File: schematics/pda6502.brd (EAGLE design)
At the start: 100 x 80 mm, 34 parts, among them IC1 74HC00D, IC2 74HC138D, IC3 DS1813-SMD, J1 CON_HEADER_2X07-PTH, U1 W65C02S, U2 W65C22S, U3 28C256, U4 UM61256AK-12

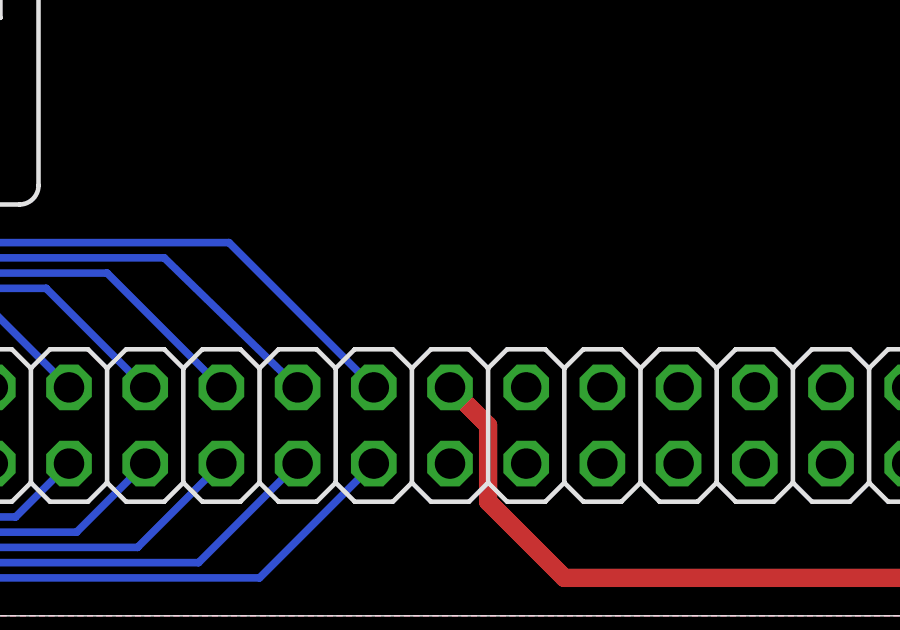
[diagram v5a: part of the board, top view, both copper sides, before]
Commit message: schematic, board: added 0.1 uF cap on 5V expansion pin 20.
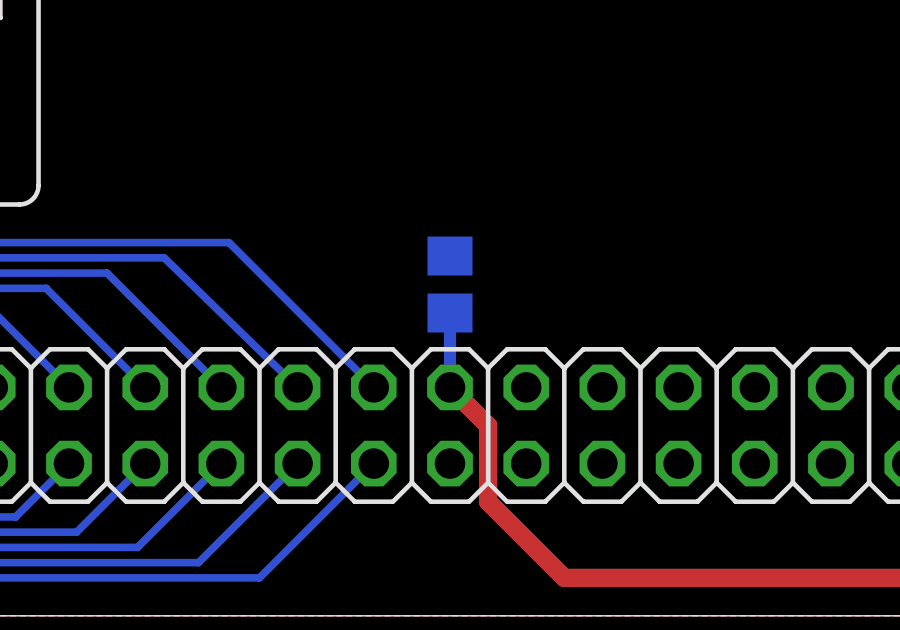
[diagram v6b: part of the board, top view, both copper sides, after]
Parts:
- added C14: 0.1μF, rcl:C0805
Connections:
- net 5V: now also C14.2
- net GND: now also C14.1
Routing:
- net 5V: track 398.3 -> 400.8 mm
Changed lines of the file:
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@@
 <element name="JP6" library="adafruit" package="2X20" value="EXPANSION" x="49.53" y="6.35"/>
 <element name="C13" library="rcl" package="C0805" value="0.1μF" x="76.962" y="5.08" rot="MR0"/>
+<element name="C14" library="rcl" package="C0805" value="0.1μF" x="48.26" y="11.049" rot="MR270"/>
 </elements>
 <signals>
@@
 <vertex x="100.33" y="80.01"/>
 </polygon>
-<wire x1="97.57" y1="69.85" x2="95.25" y2="60.96" width="0" layer="19" extent="1-1"/>
+<contactref element="C14" pad="1"/>
+<wire x1="95.25" y1="60.96" x2="97.57" y2="69.85" width="0" layer="19" extent="1-1"/>
+<wire x1="88.331" y1="60.96" x2="95.25" y2="60.96" width="0" layer="19" extent="16-16"/>
+<wire x1="81.28" y1="55.88" x2="88.331" y2="60.96" width="0" layer="19" extent="16-16"/>
+<wire x1="90.17" y1="77.8" x2="97.57" y2="69.85" width="0" layer="19" extent="1-1"/>
+<wire x1="85.09" y1="77.8" x2="90.17" y2="77.8" width="0" layer="19" extent="1-1"/>
+<wire x1="72.36" y1="76.065" x2="85.09" y2="77.8" width="0" layer="19" extent="1-1"/>
+<wire x1="66.675" y1="63.754" x2="72.39" y2="72.39" width="0" layer="19" extent="1-1"/>
+<wire x1="62.4" y1="67.31" x2="66.675" y2="63.754" width="0" layer="19" extent="1-1"/>
+<wire x1="48.26" y1="64.45" x2="62.4" y2="67.31" width="0" layer="19" extent="1-16"/>
+<wire x1="51.562" y1="51.877" x2="48.26" y2="64.45" width="0" layer="19" extent="16-16"/>
+<wire x1="47.051" y1="45.72" x2="51.562" y2="51.877" width="0" layer="19" extent="16-16"/>
+<wire x1="57.6834" y1="43.815" x2="51.562" y2="51.877" width="0" layer="19" extent="16-16"/>
+<wire x1="57.6834" y1="42.545" x2="57.6834" y2="43.815" width="0" layer="19" extent="16-16"/>
+<wire x1="57.6834" y1="38.735" x2="57.6834" y2="42.545" width="0" layer="19" extent="16-16"/>
+<wire x1="51.562" y1="35.748" x2="57.6834" y2="38.735" width="0" layer="19" extent="16-16"/>
+<wire x1="57.6834" y1="24.13" x2="51.562" y2="35.748" width="0" layer="19" extent="16-16"/>
+<wire x1="92.71" y1="45.72" x2="81.28" y2="55.88" width="0" layer="19" extent="1-1"/>
+<wire x1="95.25" y1="41.341" x2="92.71" y2="45.72" width="0" layer="19" extent="16-16"/>
+<wire x1="95.25" y1="38.1" x2="95.25" y2="41.341" width="0" layer="19" extent="16-16"/>
+<wire x1="90.744" y1="35.56" x2="95.25" y2="38.1" width="0" layer="19" extent="16-16"/>
+<wire x1="80.01" y1="31.75" x2="90.744" y2="35.56" width="0" layer="19" extent="16-16"/>
+<wire x1="75.057" y1="22.667" x2="80.01" y2="31.75" width="0" layer="19" extent="16-16"/>
+<wire x1="73.66" y1="7.62" x2="75.057" y2="22.667" width="0" layer="19" extent="16-16"/>
+<wire x1="77.912" y1="5.08" x2="73.66" y2="7.62" width="0" layer="19" extent="16-16"/>
+<wire x1="60.96" y1="7.62" x2="73.66" y2="7.62" width="0" layer="19" extent="1-1"/>
+<wire x1="55.88" y1="7.62" x2="60.96" y2="7.62" width="0" layer="19" extent="1-1"/>
+<wire x1="53.34" y1="7.62" x2="55.88" y2="7.62" width="0" layer="19" extent="1-1"/>
+<wire x1="50.8" y1="7.62" x2="53.34" y2="7.62" width="0" layer="19" extent="1-1"/>
+<wire x1="48.26" y1="5.08" x2="50.8" y2="7.62" width="0" layer="19" extent="1-1"/>
+<wire x1="35.494" y1="29.21" x2="51.562" y2="35.748" width="0" layer="19" extent="16-16"/>
+<wire x1="24.13" y1="31.75" x2="35.494" y2="29.21" width="0" layer="19" extent="16-16"/>
+<wire x1="21.59" y1="19.05" x2="24.13" y2="31.75" width="0" layer="19" extent="1-1"/>
+<wire x1="24.13" y1="16.51" x2="21.59" y2="19.05" width="0" layer="19" extent="1-1"/>
+<wire x1="25.4" y1="7.62" x2="24.13" y2="16.51" width="0" layer="19" extent="1-1"/>
+<wire x1="10.226" y1="29.21" x2="24.13" y2="31.75" width="0" layer="19" extent="16-16"/>
+<wire x1="10.16" y1="53.34" x2="10.226" y2="29.21" width="0" layer="19" extent="16-16"/>
+<wire x1="5.08" y1="62.23" x2="10.16" y2="53.34" width="0" layer="19" extent="1-1"/>
+<wire x1="5.08" y1="71.12" x2="5.08" y2="62.23" width="0" layer="19" extent="1-1"/>
+<wire x1="15.24" y1="74.93" x2="5.08" y2="71.12" width="0" layer="19" extent="1-1"/>
+<wire x1="48.26" y1="11.999" x2="25.4" y2="7.62" width="0" layer="19" extent="1-1"/>
 </signal>
 <signal name="5V">
@@
 <wire x1="76.2" y1="17.78" x2="76.2" y2="15.24" width="0.6096" layer="1"/>
 <wire x1="82.55" y1="16.51" x2="82.55" y2="8.89" width="0.3048" layer="1"/>
-<wire x1="96.52" y1="7.62" x2="93.98" y2="7.62" width="0" layer="19" extent="1-16"/>
 <wire x1="92.71" y1="3.81" x2="90.17" y2="1.27" width="0.6096" layer="1"/>
-<wire x1="93.98" y1="7.62" x2="92.71" y2="6.35" width="0" layer="19" extent="1-16"/>
 <wire x1="82.55" y1="8.89" x2="90.17" y2="1.27" width="0.6096" layer="1"/>
 <wire x1="76.012" y1="5.08" x2="73.66" y2="5.08" width="0.4064" layer="16"/>
@@
 <wire x1="95.25" y1="35.56" x2="96.52" y2="35.56" width="0.6096" layer="1"/>
 <wire x1="96.52" y1="35.56" x2="97.79" y2="36.83" width="0.6096" layer="1"/>
+<wire x1="92.71" y1="3.81" x2="92.71" y2="5.08" width="0.6096" layer="1"/>
+<wire x1="96.52" y1="7.62" x2="95.25" y2="7.62" width="0.6096" layer="1"/>
+<wire x1="92.71" y1="5.08" x2="95.25" y2="7.62" width="0.6096" layer="1" curve="-90"/>
+<contactref element="C14" pad="2"/>
+<wire x1="48.26" y1="10.099" x2="48.26" y2="7.62" width="0.4064" layer="16"/>
 <wire x1="29.21" y1="34.29" x2="31.75" y2="29.21" width="0" layer="19" extent="1-1"/>
 <wire x1="21.59" y1="28.106" x2="26.67" y2="34.29" width="0" layer="19" extent="16-16"/>
 <wire x1="13.97" y1="29.21" x2="21.59" y2="28.106" width="0" layer="19" extent="16-16"/>
 <wire x1="43.18" y1="45.72" x2="29.21" y2="34.29" width="0" layer="19" extent="16-16"/>
-<wire x1="92.71" y1="3.81" x2="92.71" y2="5.08" width="0.6096" layer="1"/>
-<wire x1="96.52" y1="7.62" x2="95.25" y2="7.62" width="0.6096" layer="1"/>
-<wire x1="92.71" y1="5.08" x2="95.25" y2="7.62" width="0.6096" layer="1" curve="-90"/>
 </signal>
 <signal name="PA0">

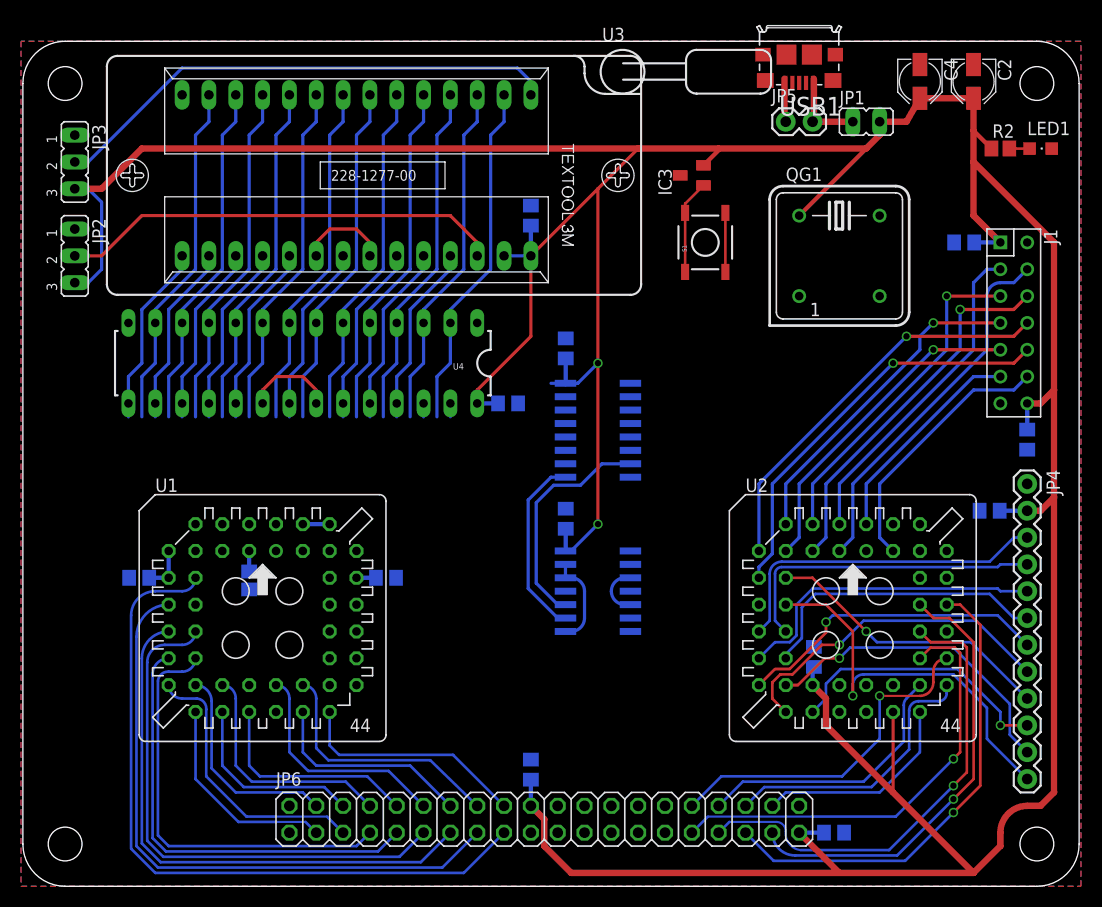
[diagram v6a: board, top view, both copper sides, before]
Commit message: board: routed ADDR[0..7, 12] down left side of board.
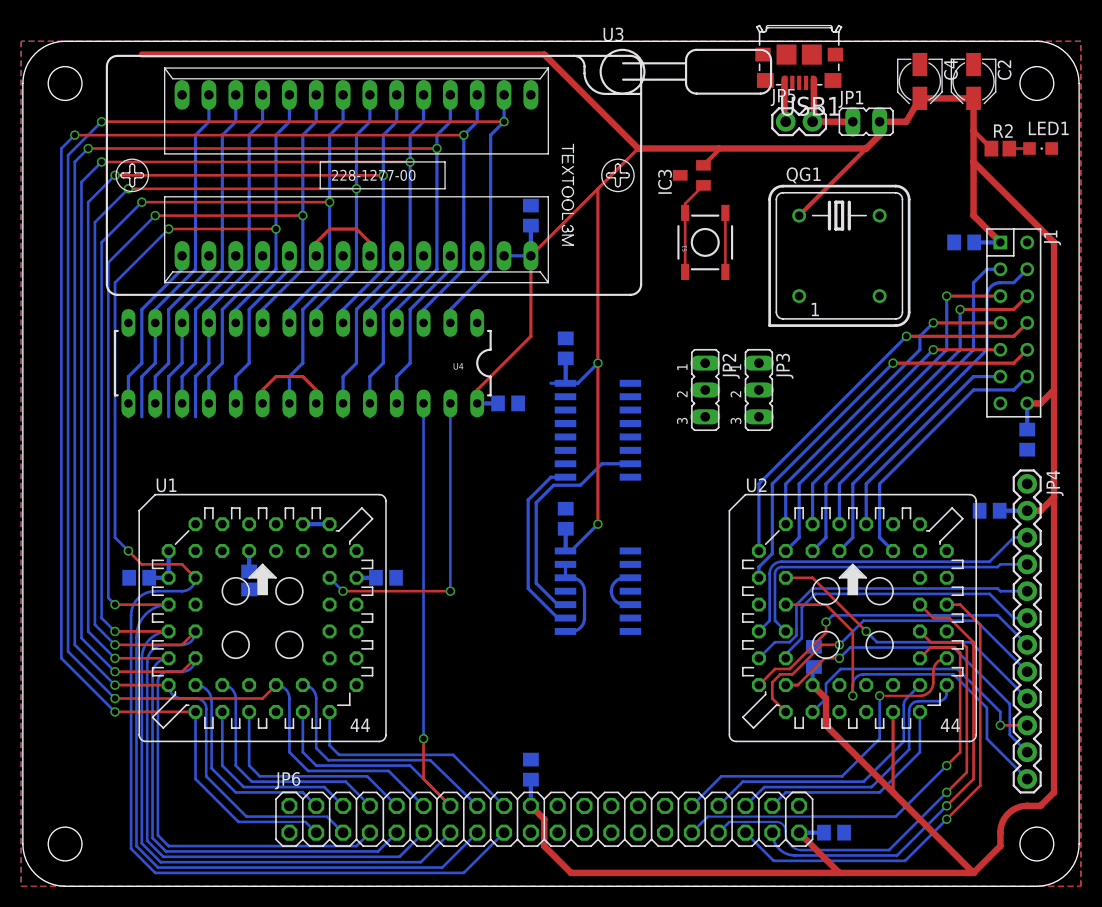
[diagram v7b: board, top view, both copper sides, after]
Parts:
- moved JP3 68.3 mm to (69.8, 47.0)
- moved JP2 61.0 mm to (64.8, 47.0)
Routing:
- net ADDR12: track 54.8 -> 157.0 mm, vias 0 -> 3
- net ADDR7: track 53.0 -> 145.3 mm, vias 0 -> 3
- net ADDR6: track 59.2 -> 140.8 mm, vias 0 -> 3
- net ADDR5: track 73.1 -> 151.4 mm, vias 0 -> 3
- net ADDR4: track 75.1 -> 144.0 mm, vias 0 -> 3
- net ADDR3: track 83.5 -> 149.1 mm, vias 0 -> 3
- net ADDR2: track 85.3 -> 141.5 mm, vias 0 -> 3
- net N$6: track 48.7 -> 0.00 mm
- net ADDR1: track 91.7 -> 140.3 mm, vias 0 -> 3
- net N$10: track 42.0 -> 0.00 mm
- net ADDR0: track 100.6 -> 141.9 mm, vias 0 -> 3
- net ADDR13: track 21.2 -> 59.0 mm, vias 0 -> 1
- net RWB: track 1.27 -> 29.7 mm, vias 0 -> 2
- net 5V: track 400.8 -> 384.1 mm
- net ADDR8: track 37.2 -> 36.0 mm

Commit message: board: trace spacing less tight; 0.025 grid for most routing.
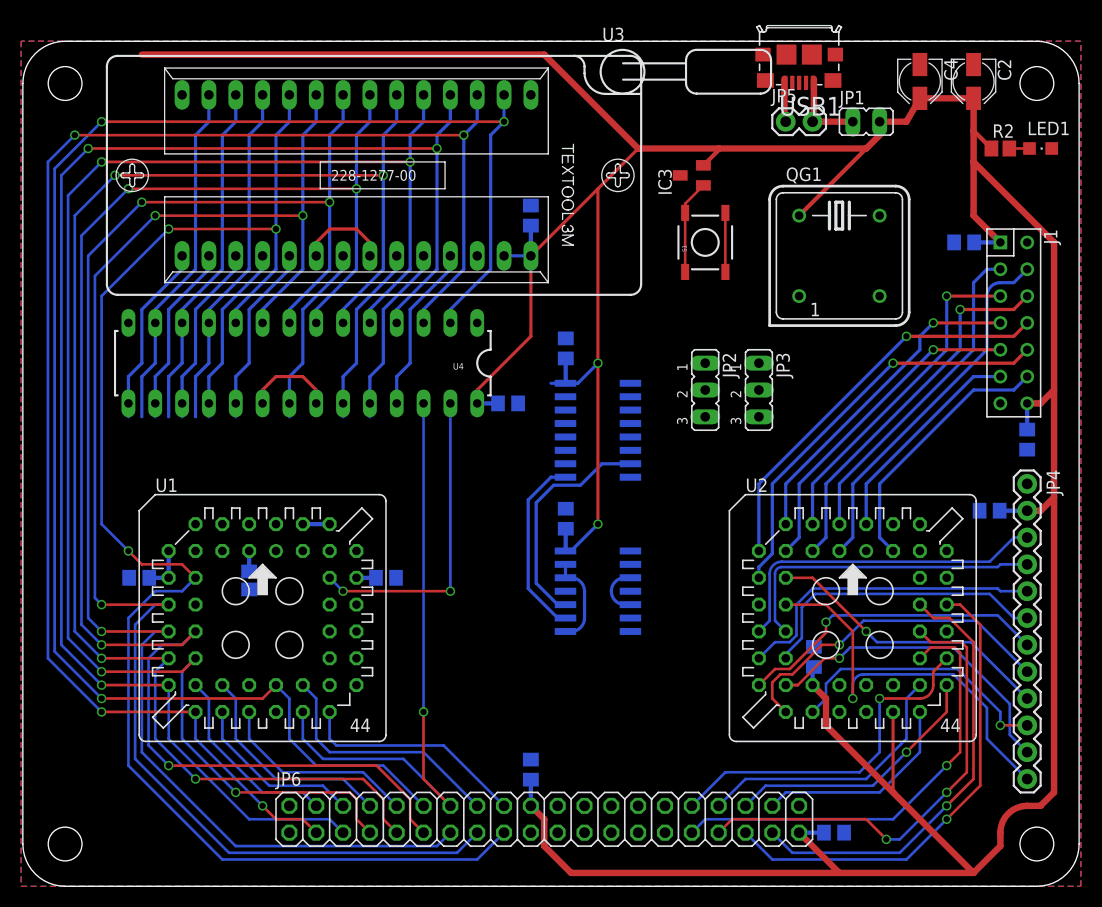
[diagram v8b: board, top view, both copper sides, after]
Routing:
- net ADDR5: track 151.4 -> 143.9 mm, vias 3 -> 4
- net ADDR4: track 144.0 -> 139.6 mm, vias 3 -> 4
- net ADDR3: track 149.1 -> 144.8 mm, vias 3 -> 4
- net ADDR0: track 141.9 -> 137.6 mm
- net ADDR2: track 141.5 -> 137.7 mm
- net ADDR1: track 140.3 -> 137.0 mm
- net ADDR9: track 35.4 -> 33.9 mm
- net ADDR11: track 38.0 -> 36.5 mm
- net ADDR10: track 39.8 -> 38.3 mm
- net ADDR8: track 36.0 -> 34.5 mm
- net DATA6: track 43.7 -> 42.6 mm, vias 0 -> 1
- net ADDR12: track 157.0 -> 158.1 mm
- net ADDR6: track 140.8 -> 141.8 mm
- net DATA2: track 78.2 -> 77.4 mm, vias 1 -> 2
- net DATA4: track 50.2 -> 51.0 mm
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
